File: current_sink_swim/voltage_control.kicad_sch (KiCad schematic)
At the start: 7 parts, among them U1 LMV358

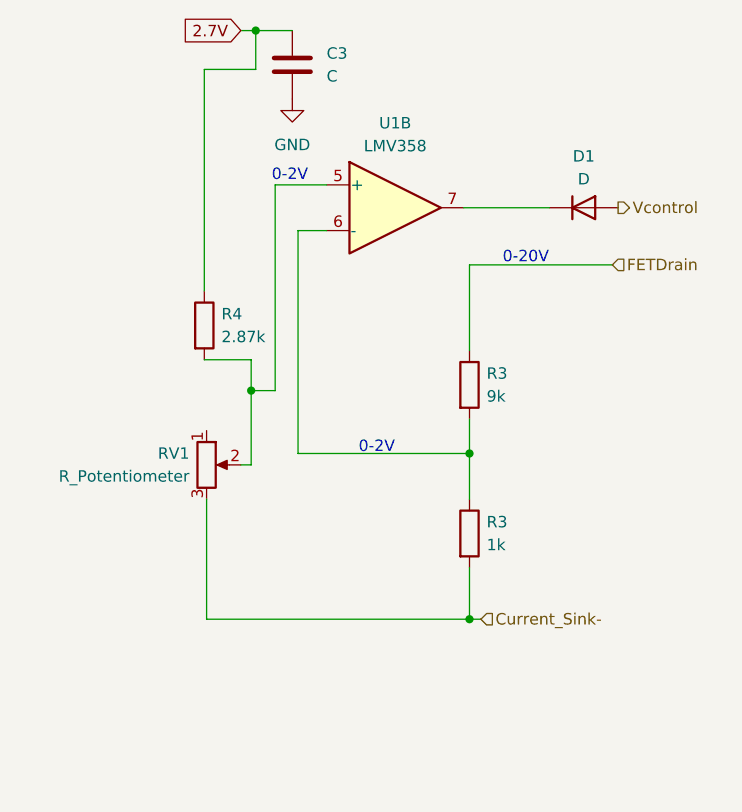
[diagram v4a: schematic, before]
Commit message: first attempt at layout. Probably will be ripped up
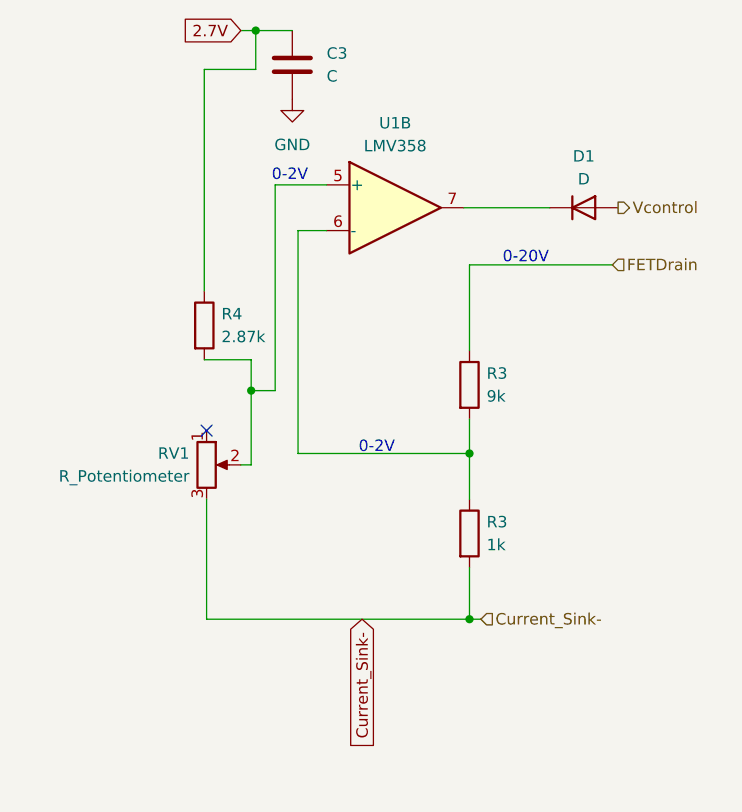
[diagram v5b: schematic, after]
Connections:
- no-connect marks 0 -> 1
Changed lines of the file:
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@@
   (junction (at 86.995 158.75) (diameter 0) (color 0 0 0 0)
   )
+  (no_connect (at 57.785 137.795))
   (wire (pts (xy 63.246 93.345) (xy 67.31 93.345))
     (stroke (width 0) (type default))
@@
       (effects (font (size 1.27 1.27)) (justify right) hide)
     )
+  )
+  (global_label "Current_Sink-" (shape input) (at 75.057 158.75 270) (fields_autoplaced)
+    (effects (font (size 1.27 1.27)) (justify right))
+    (property "Intersheetrefs" "${INTERSHEET_REFS}" (at 75.057 175.2213 90)
+      (effects (font (size 1.27 1.27)) (justify right) hide)
+    )

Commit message: add part numbers and BOM
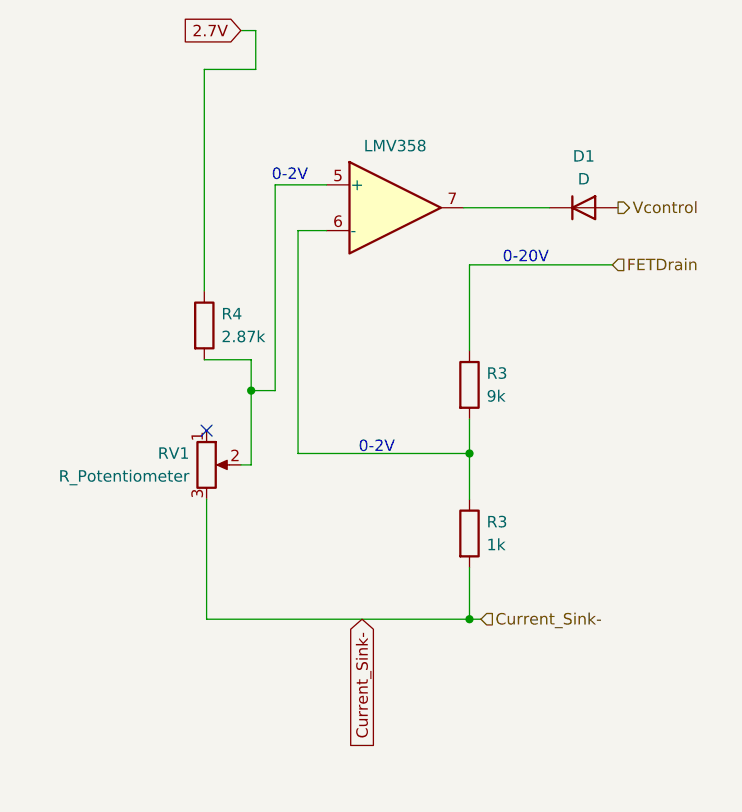
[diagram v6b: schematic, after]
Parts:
- removed C3: C, Capacitor_SMD:C_0805_2012Metric_Pad1.18x1.45mm_HandSolder, symbol Device:C
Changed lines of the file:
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@@
   (junction (at 62.738 133.35) (diameter 0) (color 0 0 0 0)
   )
-  (junction (at 63.246 93.345) (diameter 0) (color 0 0 0 0)
-  )
   (junction (at 86.995 158.75) (diameter 0) (color 0 0 0 0)
   )
   (no_connect (at 57.785 137.795))
-  (wire (pts (xy 63.246 93.345) (xy 67.31 93.345))
-    (stroke (width 0) (type default))
-  )
   (wire (pts (xy 86.36 113.03) (xy 95.885 113.03))
     (stroke (width 0) (type default))
@@
     (effects (font (size 1.27 1.27)) (justify left))
   )
-  (symbol (lib_id "power:GND") (at 67.31 100.965 0) (unit 1)
-    (in_bom yes) (on_board yes) (dnp no) (fields_autoplaced)
-    (property "Reference" "#PWR05" (at 67.31 107.315 0)
-      (effects (font (size 1.27 1.27)) hide)
-    )
-    (property "Value" "GND" (at 67.31 106.045 0)
-      (effects (font (size 1.27 1.27)))
-    )
-    (property "Footprint" "" (at 67.31 100.965 0)
-      (effects (font (size 1.27 1.27)) hide)
-    )
-    (property "Datasheet" "" (at 67.31 100.965 0)
-      (effects (font (size 1.27 1.27)) hide)
-    )
-    (pin "1")
-    (instances
-      (project "current_sink_swim"
-        (path "/d8f9bd22-1078-406d-bafe-f69bb2710c23"
-          (reference "#PWR05") (unit 1)
-        )
-        (path "/d8f9bd22-1078-406d-bafe-f69bb2710c23/7bb47634-abd5-40f7-90e5-fb54860f3e74"
-          (reference "#PWR01") (unit 1)
-        )
-        (path "/d8f9bd22-1078-406d-bafe-f69bb2710c23/114b53f6-b762-4b90-a865-8e9ebeba9179"
-          (reference "#PWR06") (unit 1)
-        )
-      )
-    )
-  )
   (symbol (lib_id "Device:R") (at 86.995 149.225 0) (unit 1)
     (in_bom yes) (on_board yes) (dnp no) (fields_autoplaced)
@@
     (in_bom yes) (on_board yes) (dnp no) (fields_autoplaced)
     (property "Reference" "U1" (at 78.74 103.632 0)
-      (effects (font (size 1.27 1.27)))
+      (effects (font (size 1.27 1.27)) hide)
     )
     (property "Value" "LMV358" (at 78.74 106.172 0)
@@
         )
       )
-    )
-  )
-  (symbol (lib_id "Device:C") (at 67.31 97.155 0) (unit 1)
-    (in_bom yes) (on_board yes) (dnp no) (fields_autoplaced)
-    (property "Reference" "C3" (at 71.12 95.885 0)
-      (effects (font (size 1.27 1.27)) (justify left))
-    )
-    (property "Value" "C" (at 71.12 98.425 0)
-      (effects (font (size 1.27 1.27)) (justify left))
-    )
-    (property "Footprint" "Capacitor_SMD:C_0805_2012Metric_Pad1.18x1.45mm_HandSolder" (at 68.2752 100.965 0)
-      (effects (font (size 1.27 1.27)) hide)
-    )
-    (property "Datasheet" "~" (at 67.31 97.155 0)
-      (effects (font (size 1.27 1.27)) hide)
-    )
-    (pin "1")
-    (pin "2")
-    (instances
-      (project "current_sink_swim"
-        (path "/d8f9bd22-1078-406d-bafe-f69bb2710c23"
-          (reference "C3") (unit 1)
-        )
-        (path "/d8f9bd22-1078-406d-bafe-f69bb2710c23/7bb47634-abd5-40f7-90e5-fb54860f3e74"
-          (reference "C3") (unit 1)
-        )
-        (path "/d8f9bd22-1078-406d-bafe-f69bb2710c23/114b53f6-b762-4b90-a865-8e9ebeba9179"
-          (reference "C2") (unit 1)
-        )
-      )
